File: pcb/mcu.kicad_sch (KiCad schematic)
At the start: 3 parts, among them U5 RP2040

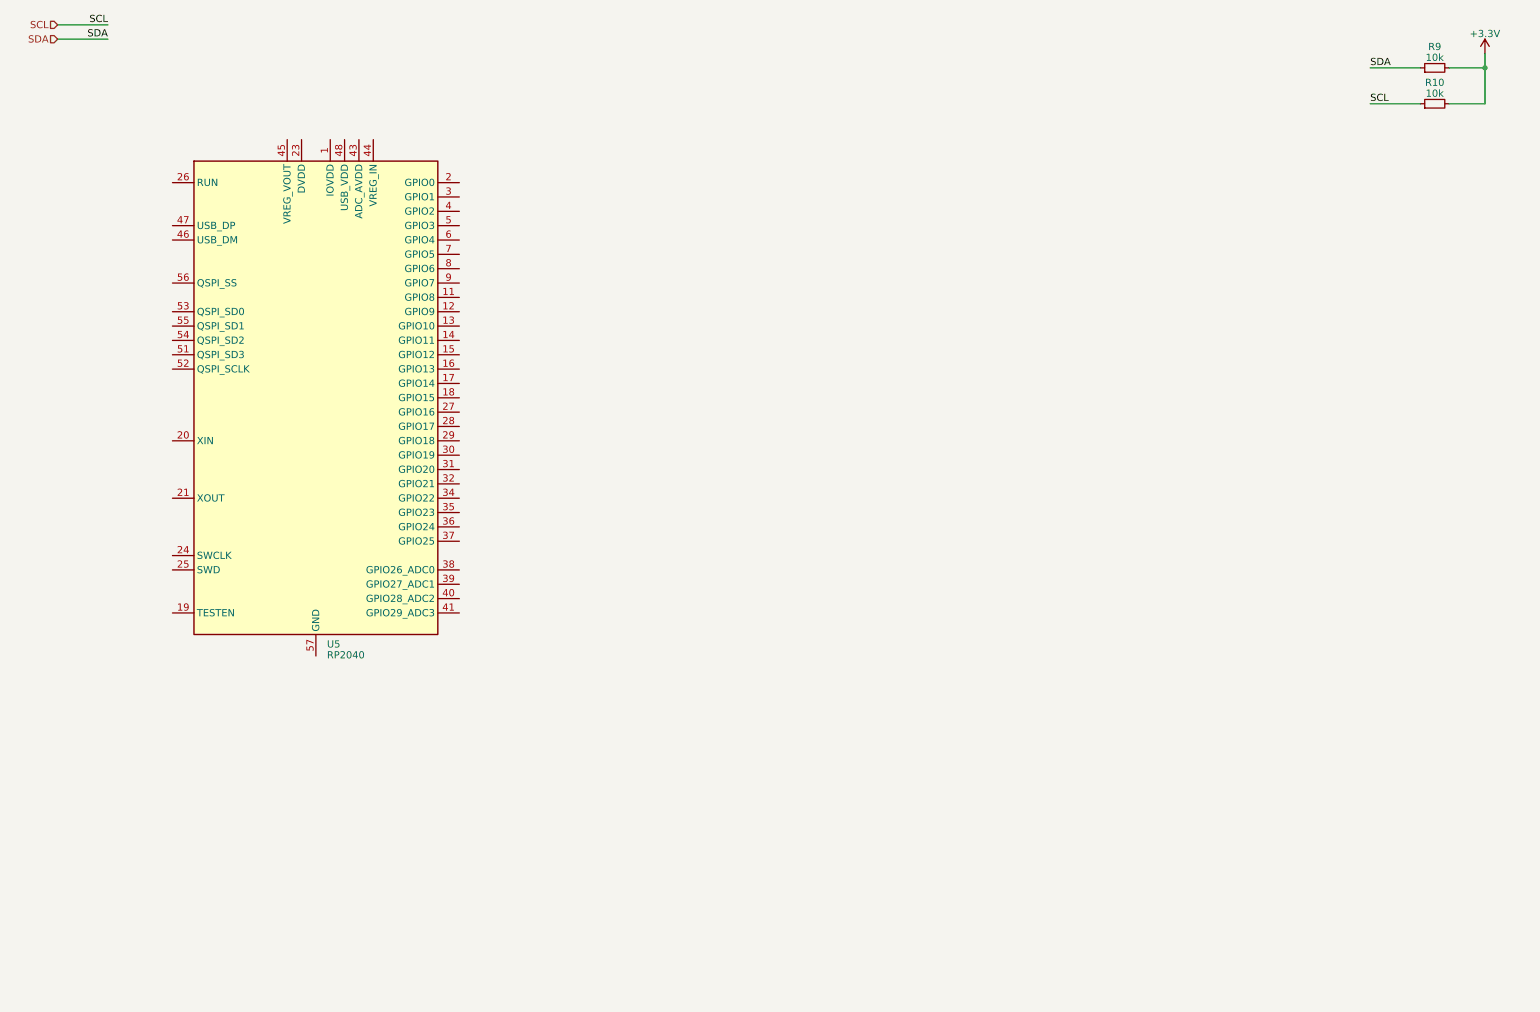
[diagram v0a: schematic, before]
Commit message: Added pcb design for first prototype
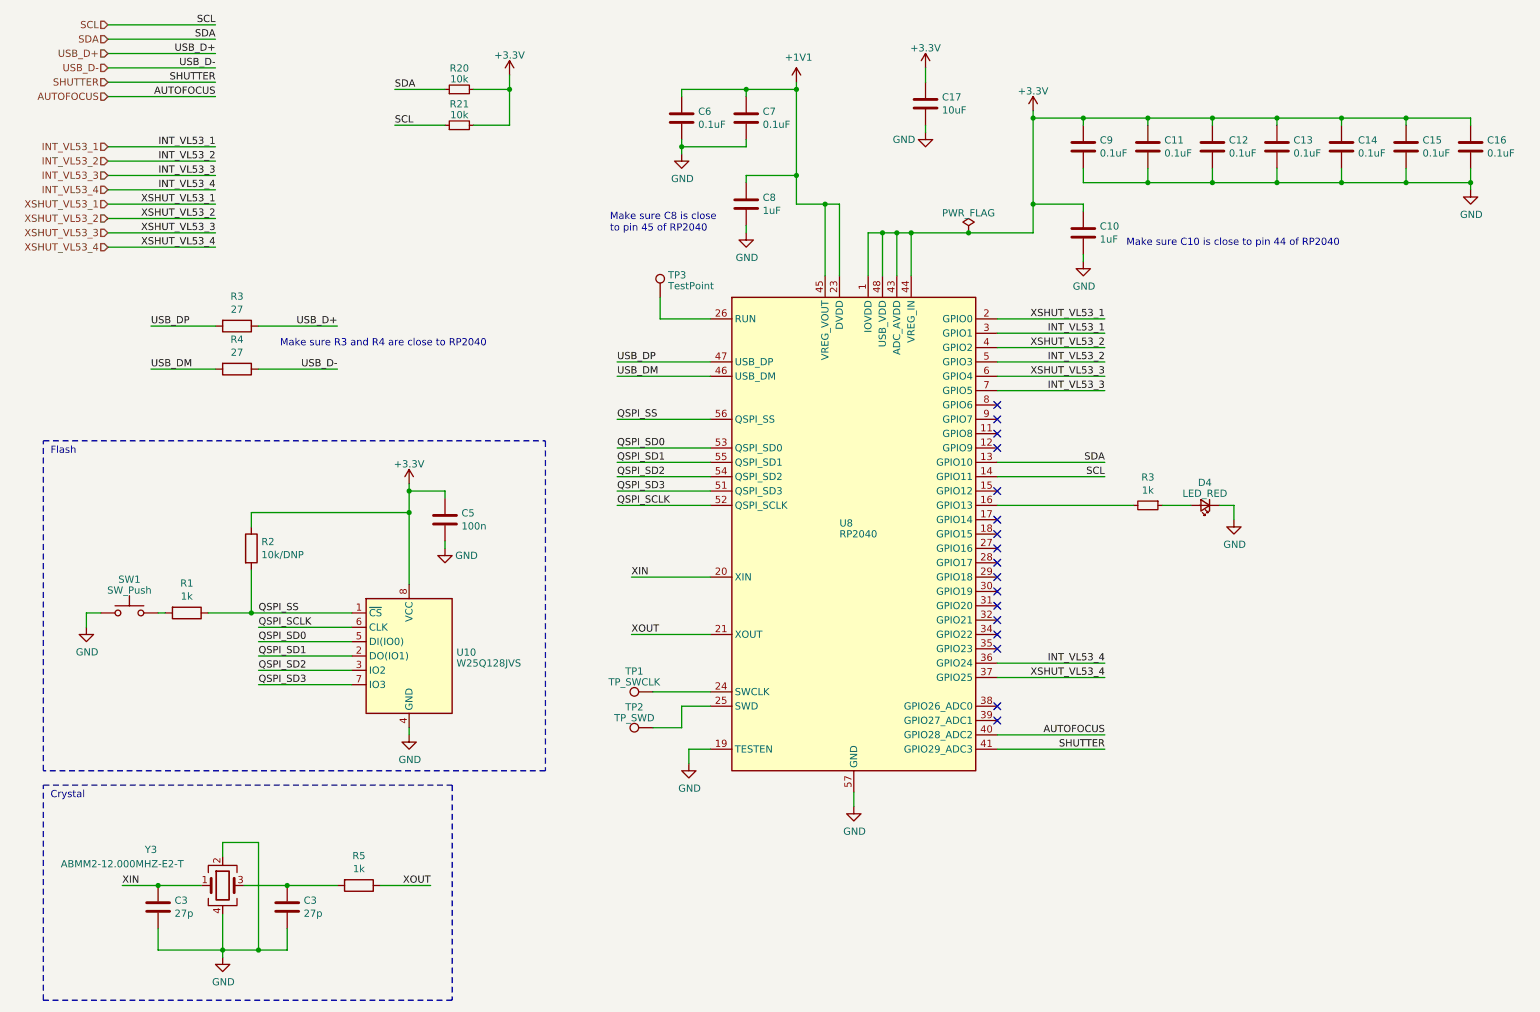
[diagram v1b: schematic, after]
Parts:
- added C10, C8: 1uF, Capacitor_SMD:C_0402_1005Metric, symbol Device:C
- added C11, C12, C13, C14, C15, C16, C6, C7, C9: 0.1uF, Capacitor_SMD:C_0402_1005Metric, symbol Device:C
- added C17: 10uF, Capacitor_SMD:C_0805_2012Metric, symbol Device:C
- added C3 (x2): 27p, Capacitor_SMD:C_0402_1005Metric, symbol Device:C
- added C5: 100n, Capacitor_SMD:C_0402_1005Metric, symbol Device:C
- added D4: LED_RED, LED_SMD:LED_0603_1608Metric, symbol Device:LED_Small
- added R1, R5: 1k, Resistor_SMD:R_0603_1608Metric, symbol Device:R
- added R2: 10k/DNP, Resistor_SMD:R_0603_1608Metric, symbol Device:R
- added R3, R4: 27, Resistor_SMD:R_0402_1005Metric, symbol Device:R
- added R3: 1k, Resistor_SMD:R_0603_1608Metric, symbol Device:R_Small
- added SW1: SW_Push, SKRKAEE020:SKRKAEE020, symbol Switch:SW_Push
- added TP1: TP_SWCLK, TestPoint:TestPoint_Pad_D1.5mm, symbol Connector:TestPoint
- added TP2: TP_SWD, TestPoint:TestPoint_Pad_D1.5mm, symbol Connector:TestPoint
- added TP3: TestPoint, TestPoint:TestPoint_Pad_D1.5mm, symbol Connector:TestPoint
- added U10: W25Q128JVS, Package_SO:SOIC-8_5.23x5.23mm_P1.27mm, symbol Memory_Flash:W25Q128JVS
- added Y3: ABMM2-12.000MHZ-E2-T, ABMM2-12.000MHZ-E2-T:ABMM2, symbol Device:Crystal_GND24
- renumbered R9 to R20, R10 to R21, U5 to U8
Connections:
- net +3.3V: now also U8.1 (IOVDD), U8.10 (IOVDD), U8.22 (IOVDD), U8.33 (IOVDD), U8.42 (IOVDD), U8.43 (ADC_AVDD), U8.44 (VREG_IN), U8.48 (USB_VDD), U8.49 (IOVDD), C10.1, C11.1, C12.1, C13.1, C14.1, C15.1, C16.1, C17.1, C5.1, C9.1, R2.1, U10.8 (VCC)
- net SCL: now also U8.14 (GPIO11)
- net SDA: now also U8.13 (GPIO10)
- net at U8.16 (GPIO13): now also R3.2
- net GND: now reaches U8.19 (TESTEN)
- net GND: now also U8.57 (GND), C10.2, C11.2, C12.2, C13.2, C14.2, C15.2, C16.2, C17.2, C3.2, C3.2, C5.2, C6.2, C7.2, C8.2, C9.2, D4.1 (K), SW1.1, U10.4 (GND), Y3.2, Y3.4
- net XSHUT_VL53_1: now reaches U8.2 (GPIO0)
- net XIN: now reaches U8.20 (XIN)
- net XIN: now also C3.1, Y3.1
- net XOUT: now reaches U8.21 (XOUT)
- net XOUT: now also R5.1
- net +1V1: now reaches U8.23 (DVDD), U8.50 (DVDD)
- net +1V1: now also U8.45 (VREG_VOUT), C6.1, C7.1, C8.1
- net at U8.24 (SWCLK): now also TP1.1
- net at U8.25 (SWD): now also TP2.1
- net at U8.26 (RUN): now also TP3.1
- net INT_VL53_1: now reaches U8.3 (GPIO1)
- net INT_VL53_4: now reaches U8.36 (GPIO24)
- net XSHUT_VL53_4: now reaches U8.37 (GPIO25)
- net XSHUT_VL53_2: now reaches U8.4 (GPIO2)
- net AUTOFOCUS: now reaches U8.40 (GPIO28_ADC2)
- net SHUTTER: now reaches U8.41 (GPIO29_ADC3)
- net USB_DM: now reaches U8.46 (USB_DM)
- net USB_DM: now also R4.2
- net USB_DP: now reaches U8.47 (USB_DP)
- net USB_DP: now also R3.2
- net INT_VL53_2: now reaches U8.5 (GPIO3)
- net QSPI_SD3: now reaches U8.51 (QSPI_SD3)
- net QSPI_SD3: now also U10.7 (IO3)
- net QSPI_SCLK: now reaches U8.52 (QSPI_SCLK)
- net QSPI_SCLK: now also U10.6 (CLK)
- net QSPI_SD0: now reaches U8.53 (QSPI_SD0)
- net QSPI_SD0: now also U10.5 (DI(IO0))
- net QSPI_SD2: now reaches U8.54 (QSPI_SD2)
- net QSPI_SD2: now also U10.3 (IO2)
- net QSPI_SD1: now reaches U8.55 (QSPI_SD1)
- net QSPI_SD1: now also U10.2 (DO(IO1))
- net QSPI_SS: now reaches U8.56 (QSPI_SS)
- net QSPI_SS: now also R1.1, R2.2, U10.1 (~{CS})
- net XSHUT_VL53_3: now reaches U8.6 (GPIO4)
- net INT_VL53_3: now reaches U8.7 (GPIO5)
- new net: C3.1, R5.2, Y3.3
- new net: D4.2 (A), R3.1
- new net: R1.2, SW1.2
- new net USB_D+: R3.1
- new net USB_D-: R4.1
- no-connect marks 0 -> 17
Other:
- note added: "Crystal"
- note added: "Flash"
- note added: "Make sure C10 is close to pin 44 of RP2040"
- note added: "Make sure C8 is close to pin 45 of RP2040"
- note added: "Make sure R3 and R4 are close to RP2040"
- moved on the sheet: R20, R21, U8

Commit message: Refactored details component namings + bom excludings
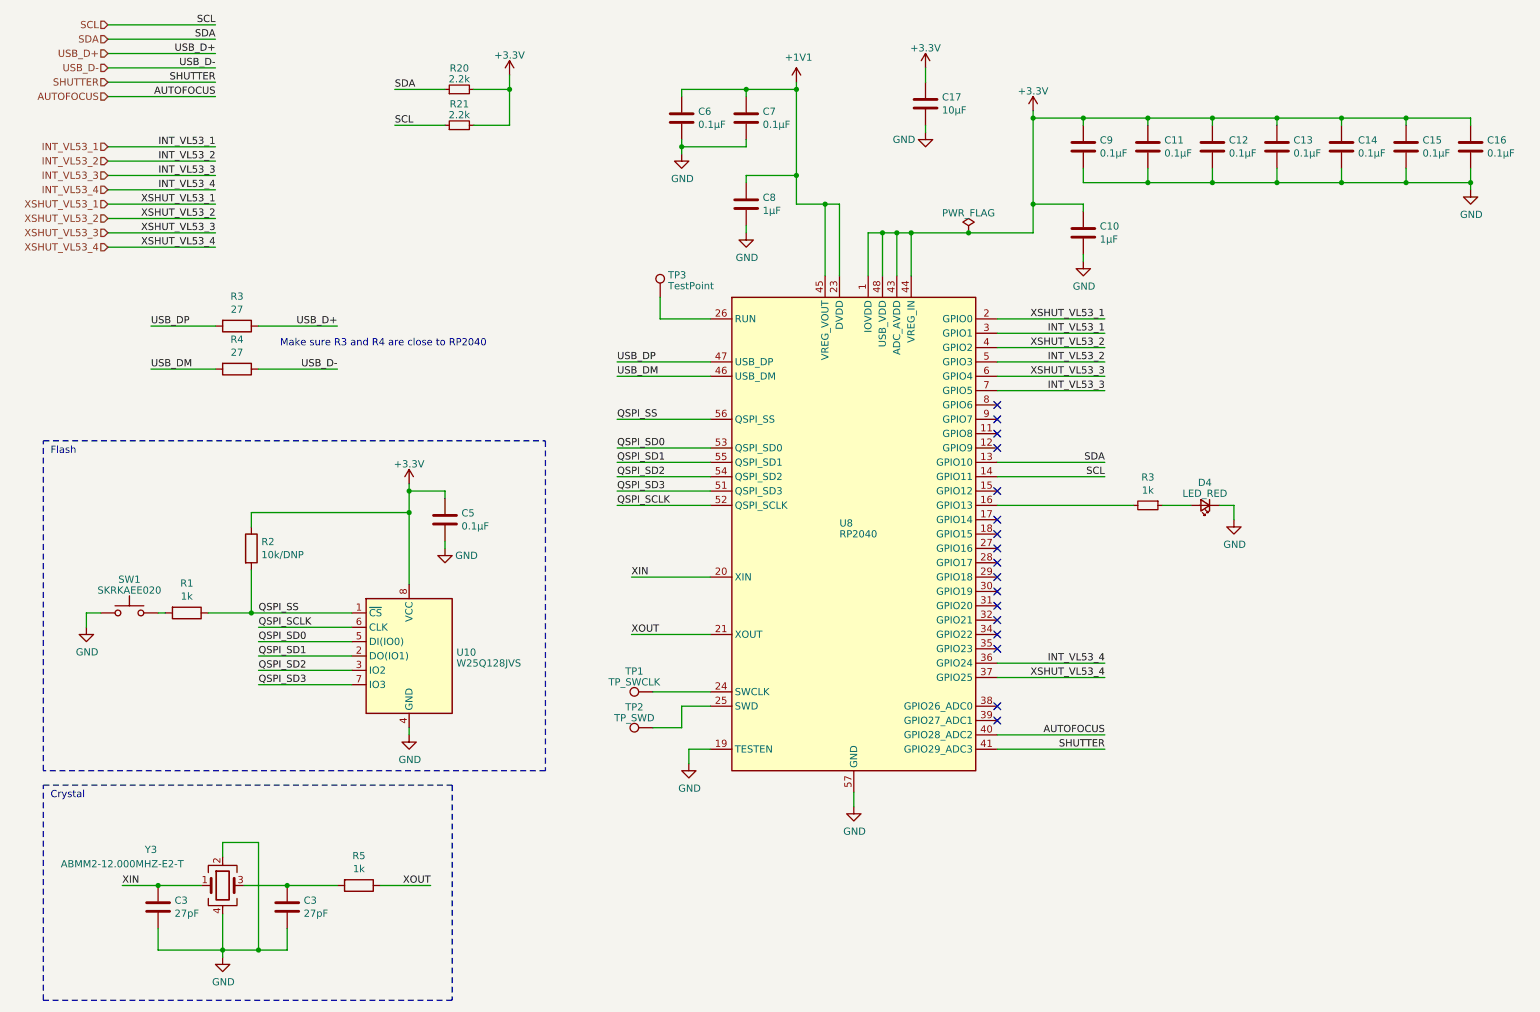
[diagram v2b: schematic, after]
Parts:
- C10, C8: value 1uF -> 1µF
- C11, C12, C13, C14, C15, C16, C6, C7, C9: value 0.1uF -> 0.1µF
- C17: value 10uF -> 10µF
- C3: value 27p -> 27pF
- C5: value 100n -> 0.1µF
- R20, R21: value 10k -> 2.2k
- SW1: value SW_Push -> SKRKAEE020
- TP1, TP2, TP3: now left out of the parts list
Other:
- note removed: "Make sure C10 is close to pin 44 of RP2040"
- note removed: "Make sure C8 is close to pin 45 of RP2040"
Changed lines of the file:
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@@
-    (effects (font (size 1.27 1.27)) (justify left bottom))
-  )
-  (text "Make sure C10 is close to pin 44 of RP2040" (at 209.55 55.88 0)
-    (effects (font (size 1.27 1.27)) (justify left bottom))
-  )
-  (text "Make sure C8 is close \nto pin 45 of RP2040" (at 118.11 53.34 0)
     (effects (font (size 1.27 1.27)) (justify left bottom))
   )
@@
       (effects (font (size 1.27 1.27)))
     )
-    (property "Value" "10k" (at 91.44 32.4645 90)
+    (property "Value" "2.2k" (at 91.44 32.4645 90)
       (effects (font (size 1.27 1.27)))
     )
@@
       (effects (font (size 1.27 1.27)) (justify left))
     )
-    (property "Value" "0.1uF" (at 133.731 34.163 0)
+    (property "Value" "0.1µF" (at 133.731 34.163 0)
       (effects (font (size 1.27 1.27)) (justify left))
     )
@@
       (effects (font (size 1.27 1.27)) (justify left))
     )
-    (property "Value" "0.1uF" (at 204.851 39.243 0)
+    (property "Value" "0.1µF" (at 204.851 39.243 0)
       (effects (font (size 1.27 1.27)) (justify left))
     )
@@
       (effects (font (size 1.27 1.27)) (justify left))
     )
-    (property "Value" "100n" (at 91.821 105.283 0)
+    (property "Value" "0.1µF" (at 91.821 105.283 0)
       (effects (font (size 1.27 1.27)) (justify left))
     )
@@
   )
   (symbol (lib_id "Connector:TestPoint") (at 127 64.77 0) (unit 1)
-    (in_bom yes) (on_board yes) (dnp no) (fields_autoplaced)
+    (in_bom no) (on_board yes) (dnp no) (fields_autoplaced)
     (property "Reference" "TP3" (at 128.397 60.8243 0)
       (effects (font (size 1.27 1.27)) (justify left))
@@
       (effects (font (size 1.27 1.27)) (justify left))
     )
-    (property "Value" "27p" (at 63.881 173.863 0)
+    (property "Value" "27pF" (at 63.881 173.863 0)
       (effects (font (size 1.27 1.27)) (justify left))
     )
@@
       (effects (font (size 1.27 1.27)) (justify left))
     )
-    (property "Value" "1uF" (at 145.161 49.403 0)
+    (property "Value" "1µF" (at 145.161 49.403 0)
       (effects (font (size 1.27 1.27)) (justify left))
     )
@@
       (effects (font (size 1.27 1.27)))
     )
-    (property "Value" "SW_Push" (at 33.02 116.6401 0)
+    (property "Value" "SKRKAEE020" (at 33.02 116.6401 0)
       (effects (font (size 1.27 1.27)))
     )
@@
       (effects (font (size 1.27 1.27)))
     )
-    (property "Value" "10k" (at 91.44 26.1145 90)
+    (property "Value" "2.2k" (at 91.44 26.1145 90)
       (effects (font (size 1.27 1.27)))
     )
@@
       (effects (font (size 1.27 1.27)) (justify left))
     )
-    (property "Value" "27p" (at 41.021 173.863 0)
+    (property "Value" "27pF" (at 41.021 173.863 0)
       (effects (font (size 1.27 1.27)) (justify left))
     )
@@
   )
   (symbol (lib_id "Connector:TestPoint") (at 125.73 140.97 90) (unit 1)
-    (in_bom yes) (on_board yes) (dnp no) (fields_autoplaced)
+    (in_bom no) (on_board yes) (dnp no) (fields_autoplaced)
     (property "Reference" "TP2" (at 122.428 137.3251 90)
       (effects (font (size 1.27 1.27)))
@@
   )
   (symbol (lib_id "Connector:TestPoint") (at 125.73 134.62 90) (unit 1)
-    (in_bom yes) (on_board yes) (dnp no) (fields_autoplaced)
+    (in_bom no) (on_board yes) (dnp no) (fields_autoplaced)
     (property "Reference" "TP1" (at 122.428 130.9751 90)
       (effects (font (size 1.27 1.27)))
@@
       (effects (font (size 1.27 1.27)) (justify left))
     )
-    (property "Value" "0.1uF" (at 227.711 39.243 0)
+    (property "Value" "0.1µF" (at 227.711 39.243 0)
       (effects (font (size 1.27 1.27)) (justify left))
     )
@@
       (effects (font (size 1.27 1.27)) (justify left))
     )
-    (property "Value" "0.1uF" (at 145.161 34.163 0)
+    (property "Value" "0.1µF" (at 145.161 34.163 0)
       (effects (font (size 1.27 1.27)) (justify left))
     )
@@
       (effects (font (size 1.27 1.27)) (justify left))
     )
-    (property "Value" "0.1uF" (at 262.001 39.243 0)
+    (property "Value" "0.1µF" (at 262.001 39.243 0)
       (effects (font (size 1.27 1.27)) (justify left))
     )
@@
       (effects (font (size 1.27 1.27)) (justify left))
     )
-    (property "Value" "0.1uF" (at 216.281 39.243 0)
+    (property "Value" "0.1µF" (at 216.281 39.243 0)
       (effects (font (size 1.27 1.27)) (justify left))
     )
@@
       (effects (font (size 1.27 1.27)) (justify left))
     )
-    (property "Value" "0.1uF" (at 250.571 39.243 0)
+    (property "Value" "0.1µF" (at 250.571 39.243 0)
       (effects (font (size 1.27 1.27)) (justify left))
     )
@@
       (effects (font (size 1.27 1.27)) (justify left))
     )
-    (property "Value" "0.1uF" (at 239.141 39.243 0)
+    (property "Value" "0.1µF" (at 239.141 39.243 0)
       (effects (font (size 1.27 1.27)) (justify left))
     )
@@
       (effects (font (size 1.27 1.27)) (justify left))
     )
-    (property "Value" "0.1uF" (at 273.431 39.243 0)
+    (property "Value" "0.1µF" (at 273.431 39.243 0)
       (effects (font (size 1.27 1.27)) (justify left))
     )
@@
       (effects (font (size 1.27 1.27)) (justify left))
     )
-    (property "Value" "1uF" (at 204.851 54.483 0)
+    (property "Value" "1µF" (at 204.851 54.483 0)
       (effects (font (size 1.27 1.27)) (justify left))
     )
@@
       (effects (font (size 1.27 1.27)) (justify left))
     )
-    (property "Value" "10uF" (at 176.911 31.623 0)
-      (effects (font (size 1.27 1.27)) (justify left))
-    )
+    (property "Value" "10µF" (at 176.911 31.623 0)
+      (effects (font (size 1.27 1.27)) (justify left))
+    )

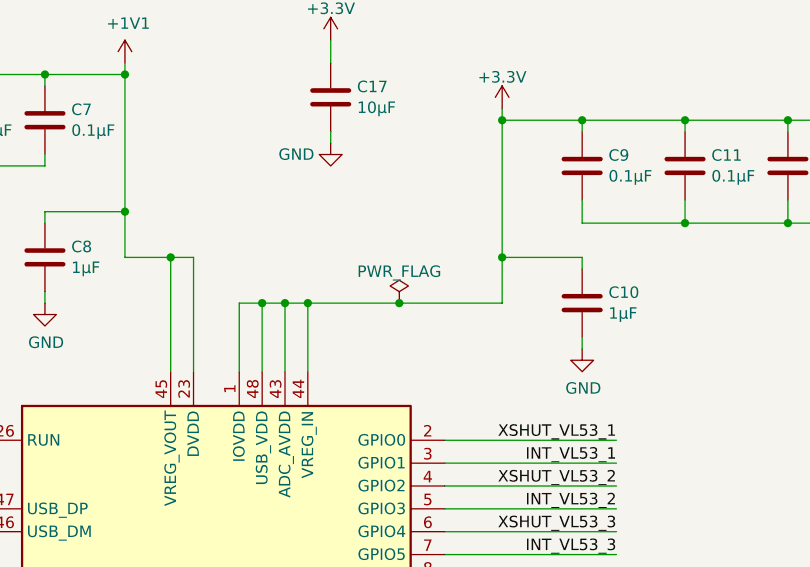
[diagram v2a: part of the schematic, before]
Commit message: Applied ERC issue changes + DRC issues fix
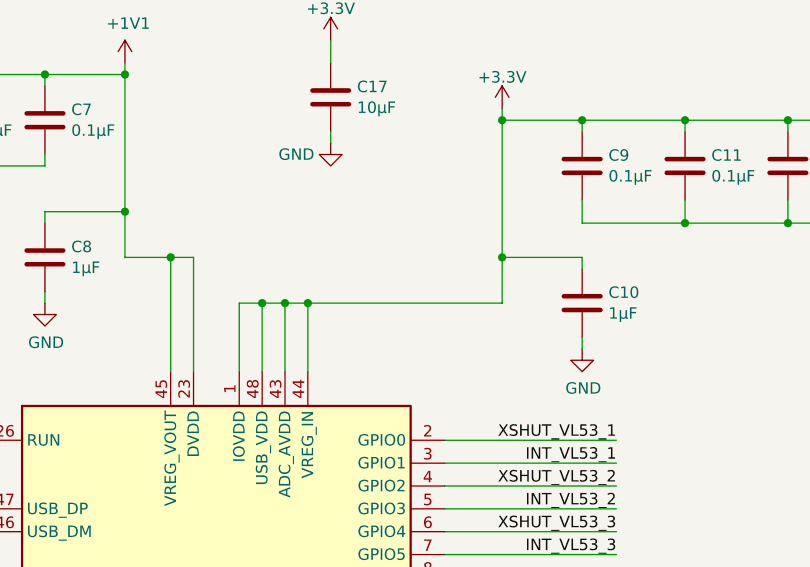
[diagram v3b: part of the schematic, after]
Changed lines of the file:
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@@
   (junction (at 236.22 33.02) (diameter 0) (color 0 0 0 0)
-  )
-  (junction (at 181.61 53.34) (diameter 0) (color 0 0 0 0)
   )
   (junction (at 247.65 33.02) (diameter 0) (color 0 0 0 0)
@@
     (stroke (width 0) (type default))
   )
-  (wire (pts (xy 171.45 53.34) (xy 181.61 53.34))
+  (wire (pts (xy 171.45 53.34) (xy 193.04 53.34))
     (stroke (width 0) (type default))
   )
@@
   )
   (wire (pts (xy 36.83 77.47) (xy 48.26 77.47))
-    (stroke (width 0) (type default))
-  )
-  (wire (pts (xy 181.61 53.34) (xy 193.04 53.34))
     (stroke (width 0) (type default))
   )
@@
         )
       )
-    )
-  )
-  (symbol (lib_id "power:PWR_FLAG") (at 181.61 53.34 0) (unit 1)
-    (in_bom yes) (on_board yes) (dnp no) (fields_autoplaced)
-    (property "Reference" "#FLG03" (at 181.61 51.435 0)
-      (effects (font (size 1.27 1.27)) hide)
-    )
-    (property "Value" "PWR_FLAG" (at 181.61 49.8381 0)
-      (effects (font (size 1.27 1.27)))
-    )
-    (property "Footprint" "" (at 181.61 53.34 0)
-      (effects (font (size 1.27 1.27)) hide)
-    )
-    (property "Datasheet" "~" (at 181.61 53.34 0)
-      (effects (font (size 1.27 1.27)) hide)
-    )
-    (pin "1")
-    (instances
-      (project "rep-trap-pcb"
-        (path "/b363dc8f-4a45-4779-a397-ccb82393dab8/eebb1d37-a01d-4adf-be70-a8e8f9293475/e7ccec12-46ad-495a-887c-7169982423a2"
-          (reference "#FLG03") (unit 1)
-        )
-      )
